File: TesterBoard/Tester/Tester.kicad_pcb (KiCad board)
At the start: 2 copper layers, 147 parts, among them J1 Conn_01x03_Pin, J2 PJ-102A, J3 Conn_01x03_Pin, J4 Conn_01x02_Pin, J5 Conn_01x02_Pin, J6 Conn_01x02_Pin, J7 Conn_01x02_Pin, J8 Conn_01x16_Pin, J9 Conn_01x08_Pin, SW1 SW_Push, SW10 SW_Push, SW2 SW_Push, SW3 SW_Push, SW4 SW_Push, SW5 SW_Push, SW6 SW_Push, SW7 SW_Push, SW8 SW_Push, U1 L7805, U10 74HC244, U2 Z80CPU, U3 74LS14, U4 sn74ls32n, U5 CY62256-70PC, U6 LCD-16X2, U7 SST39SF010, U8 74HC138, U9 74HC00, Y1 ACH-4.000MHZ-EK

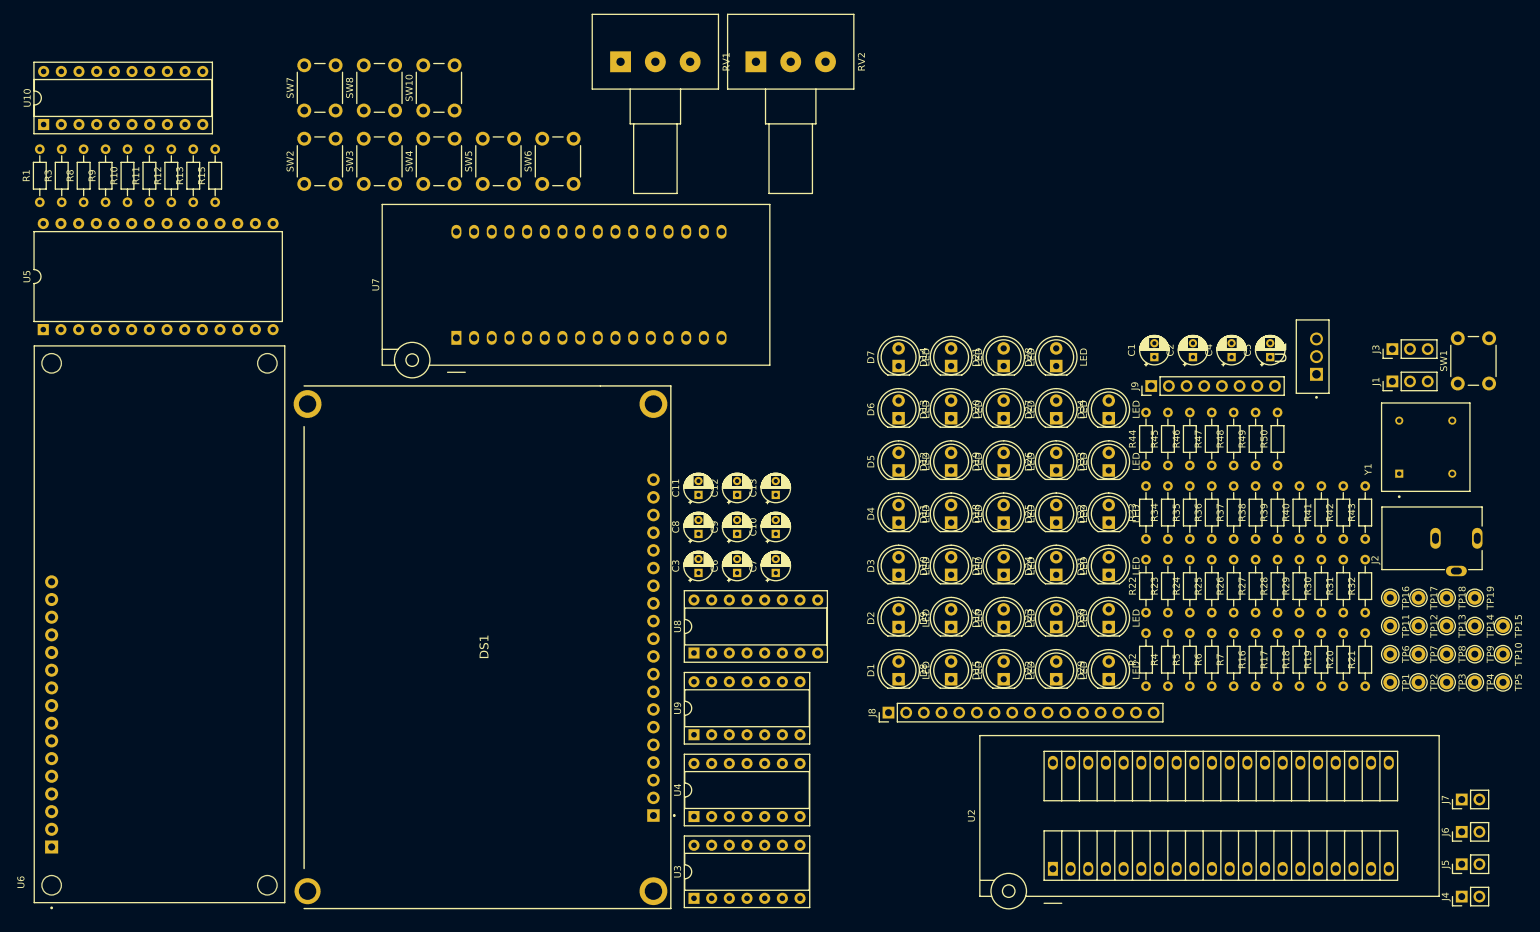
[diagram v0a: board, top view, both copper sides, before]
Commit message: updated PCB to fix logic, ready to place and route
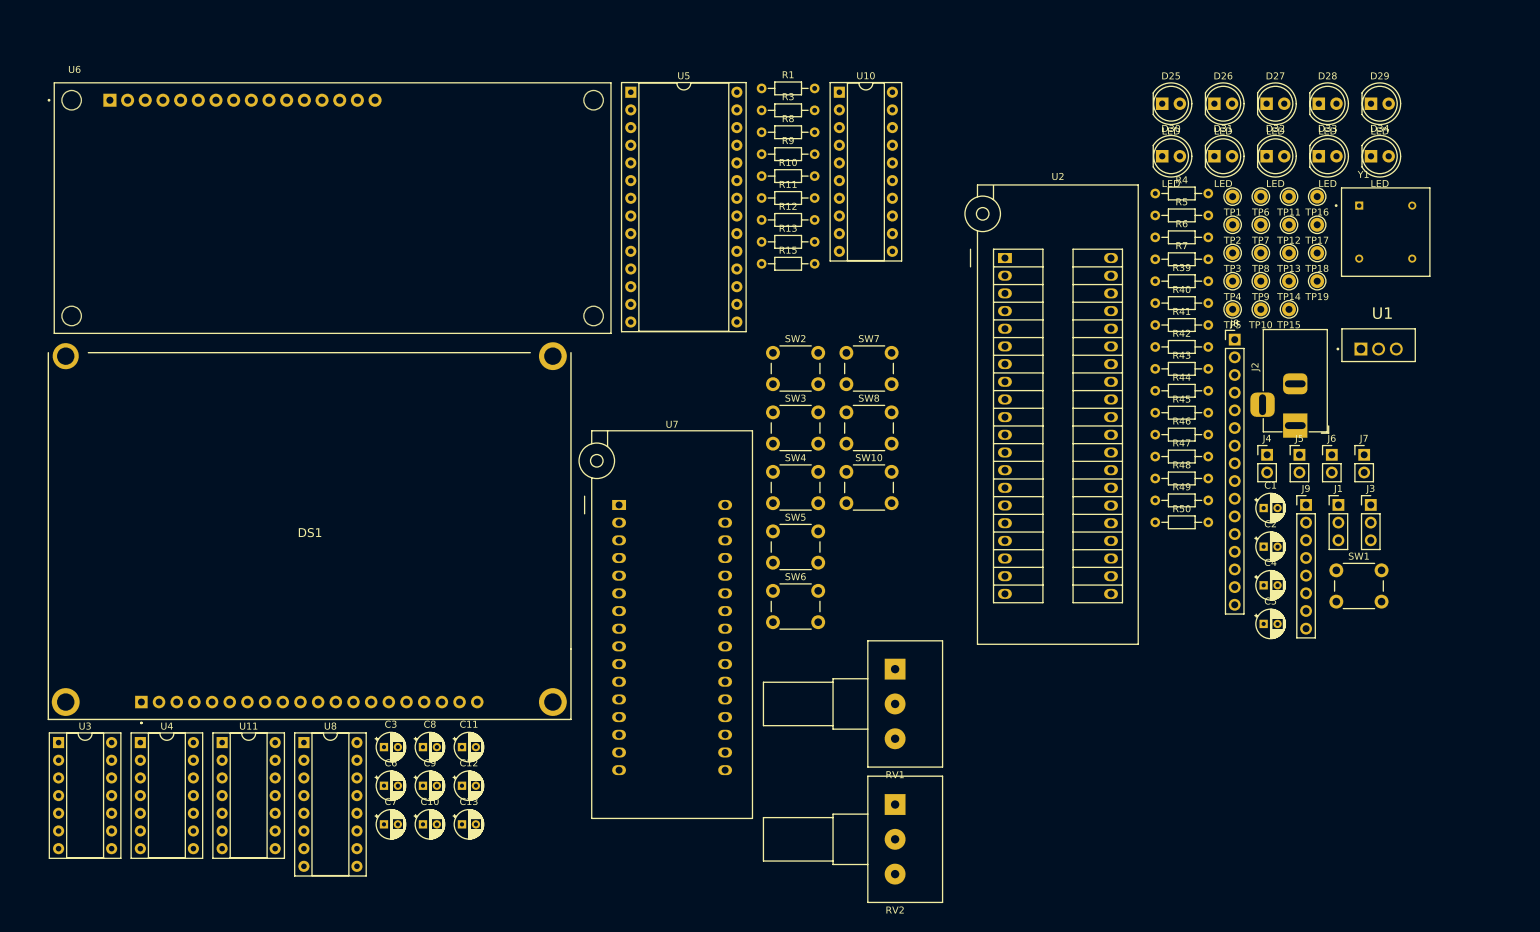
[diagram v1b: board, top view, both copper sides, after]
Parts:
- removed D1, D10, D11, D12, D13, D14, D15, D16, D17, D18, D19, D2, D20, D21, D22, D23, D24, D3, D4, D5, D6, D7, D8, D9: LED, ECE445L:LED_D5.0mm
- removed R16, R17, R18, R19, R2, R20, R21, R22, R23, R24, R25, R26, R27, R28, R29, R30, R31, R32, R33, R34, R35, R36, R37, R38: 1K, ECE445L:R_Axial_DIN0204_L3.6mm_D1.6mm_P7.62mm_Horizontal
- removed U9: 74HC00, Package_DIP:DIP-14_W7.62mm_Socket
- added U11: 74LS32, Package_DIP:DIP-14_W7.62mm_Socket, F.Cu at (69.3, 128.1)
- J2: footprint Z80_Tester_Footprints:CUI_PJ-102A -> Connector_BarrelJack:BarrelJack_Horizontal
- U4: value sn74ls32n -> 74LS02
- U5: footprint Package_DIP:DIP-28_W15.24mm -> Package_DIP:DIP-28_W15.24mm_Socket
- moved U10 114.4 mm to (158.0, 34.6), turned to 0 degrees
- moved RV2 108.6 mm to (166.0, 136.9), turned to 0 degrees
- moved R1 105.0 mm to (146.8, 34.0), turned to 0 degrees
- moved R3 101.4 mm to (146.8, 37.2), turned to 0 degrees
- moved R8 97.9 mm to (146.8, 40.4), turned to 0 degrees
- moved RV1 95.8 mm to (166.0, 117.5), turned to 0 degrees
- moved R9 94.5 mm to (146.8, 43.5), turned to 0 degrees
- moved U3 94.0 mm to (45.8, 128.1), turned to 0 degrees
- moved R10 91.2 mm to (146.8, 46.6), turned to 0 degrees
- moved U5 91.0 mm to (128.0, 34.6), turned to 0 degrees
- moved D29 90.9 mm to (234.4, 36.2), turned to 0 degrees
- moved U2 88.0 mm to (181.8, 58.4), turned to 0 degrees
- moved R11 88.0 mm to (146.8, 49.8), turned to 0 degrees
- moved SW7 85.3 mm to (159.0, 72.0), turned to 0 degrees
- moved R12 84.9 mm to (146.8, 53.0), turned to 0 degrees
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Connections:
- U4 pad 1: /WR -> 1602_Enable
- U4 pad 10: (no net) -> unconnected-(U4-Pad10)
- U4 pad 11: (no net) -> +5V
- U4 pad 12: (no net) -> +5V
- U4 pad 13: (no net) -> unconnected-(U4-Pad13)
- U4 pad 14: (no net) -> +5V
- U4 pad 2: /MREQ -> /1602_Select
- U4 pad 3: Net-(U5-~{OE}) -> /WR
- U4 pad 4: GND -> 12864_Enable
- U4 pad 5: /MREQ -> /12864_Select
- U4 pad 6: /RD -> /WR
- U4 pad 7: Net-(U5-~{WE}) -> GND
- U4 pad 9: (no net) -> +5V

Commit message: minor changes to pcb : labels for schematic
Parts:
- moved U6 182.9 mm to (-86.4, -12.0)
- moved DS1 175.8 mm to (-110.7, 71.8)
- moved C10 161.3 mm to (-58.0, 180.2)
- moved C11 161.3 mm to (-52.4, 169.1)
- moved C12 161.3 mm to (-52.4, 174.7)
- moved C13 161.3 mm to (-52.4, 180.2)
- moved C3 161.3 mm to (-63.6, 169.1)
- moved C6 161.3 mm to (-63.6, 174.7)
- moved C7 161.3 mm to (-63.6, 180.2)
- moved C8 161.3 mm to (-58.0, 169.1)
- moved C9 161.3 mm to (-58.0, 174.7)
- moved U11 161.3 mm to (-86.8, 168.5)
- moved U3 161.3 mm to (-110.3, 168.5)
- moved U4 161.3 mm to (-98.6, 168.5)
- moved U8 161.3 mm to (-75.1, 168.5)
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
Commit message: Placed PCB awaiting review
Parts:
- D25, D26, D27, D28, D29, D30, D31, D32, D33, D34, DS1, R1, R10, R11, R12, R13, R15, R39, R41, R42, R43, R44, R45, R46, R47, R48, R49, R50, R8, R9, RV1, RV2, SW1, SW10, SW2, SW3, SW4, SW5, SW6, SW7, SW8, U6: moved to B.Cu
- moved C7 312.7 mm to (205.0, 20.0)
- moved U3 307.2 mm to (169.4, 41.5)
- moved C6 296.9 mm to (223.0, 97.0)
- moved U4 277.7 mm to (171.4, 103.4)
- moved U11 267.4 mm to (148.4, 41.3)
- moved C3 258.5 mm to (153.0, 28.0)
- moved C8 257.8 mm to (153.0, 21.0)
- moved DS1 254.2 mm to (133.6, 142.0)
- moved U8 234.6 mm to (150.2, 103.1)
- moved GND 234.5 mm to (24.0, 114.0)
- moved C11 229.2 mm to (174.0, 133.0), turned to 90 degrees
- moved GND 222.4 mm to (81.0, 139.0)
- moved /Halt 217.2 mm to (79.0, 63.0)
- moved J3 214.2 mm to (23.1, 128.8), turned to 180 degrees
- moved /M1 206.8 mm to (79.0, 56.0)
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- renumbered TP4 to /Halt, TP10 to /INT, TP8 to /IOREQ, TP3 to /M1, TP7 to /MREQ, TP9 to /NMI, TP5 to /RD, TP1 to /Reset, TP11 to /WAIT, TP6 to /WR, TP19 to GND, TP18 to GND, TP14 to GND, TP17 to GND, TP12 to GND, TP16 to GND, TP13 to GND, TP15 to GND
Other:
- board outline added: 209.1 x 127 mm
- board text added: "5V Jump"
- board text added: "External 5V"
- board text added: "External Clock"
- board text added: "External GND"
- board text added: "IO 3-8 Decoder"
- board text added: "IO Enable Logic"
- board text added: "LCD"
- board text added: "Memory"
- board text added: "Oscillator"
- board text added: "Power In"
- board text added: "Reset"
- board text added: "SRAM"
- board text added: "Schmitt Trigger Inverter"
- board text added: "Unused LCD"
- board text added: "Z80"

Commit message: Almost done routing
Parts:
- added H1: ~, ECE445L:MountingHole_4_40, F.Cu at (259.2, 22.0)
- added H2: ~, ECE445L:MountingHole_4_40, F.Cu at (258.9, 150.6)
- added H3: ~, ECE445L:MountingHole_4_40, F.Cu at (24.8, 152.0)
- added H4: ~, ECE445L:MountingHole_4_40, F.Cu at (25.5, 21.9)
- moved C7 86.3 mm to (256.6, 89.3)
- moved D34 85.9 mm to (144.0, 61.2), turned to 0 degrees
- moved D31 77.6 mm to (144.1, 49.0), turned to 0 degrees
- moved D33 74.7 mm to (135.3, 61.2), turned to 0 degrees
- moved C4 72.5 mm to (136.5, 132.8), turned to 180 degrees
- moved TP17 71.6 mm to (143.2, 132.5), turned to 180 degrees
- moved D30 66.4 mm to (135.0, 49.0), turned to 0 degrees
- moved D26 62.9 mm to (125.8, 61.2), turned to 0 degrees
- moved D29 55.1 mm to (125.8, 49.0), turned to 0 degrees
- moved D32 50.8 mm to (116.0, 61.2), turned to 0 degrees
- moved TP4 44.3 mm to (117.6, 41.2)
- moved D28 43.7 mm to (116.3, 49.0), turned to 0 degrees
- moved SW8 42.8 mm to (73.5, 137.5)
- moved J1 41.6 mm to (184.4, 91.8)
- moved R40 41.6 mm to (199.2, 82.7)
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- renumbered /Reset to TP1, /INT to TP10, /WAIT to TP11, GND to TP12, GND to TP13, GND to TP14, GND to TP15, GND to TP16, GND to TP17, GND to TP18, GND to TP19, /M1 to TP3, /Halt to TP4, /RD to TP5, /WR to TP6, /MREQ to TP7, /IOREQ to TP8, /NMI to TP9
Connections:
- U3 pad 8: /Buttons_Enable -> unconnected-(U3-Pad8)
- U3 pad 9: Buttons_Enable -> +5V
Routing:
- net GND: track 0.00 -> 1171.3 mm, vias 0 -> 1
- net +5V: track 0.00 -> 954.4 mm
- net B7: track 0.00 -> 250.7 mm, vias 0 -> 7
- net Address3: track 0.00 -> 228.6 mm, vias 0 -> 1
- net /Buttons_Enable: track 0.00 -> 225.7 mm, vias 0 -> 11
- net Data4: track 0.00 -> 216.8 mm, vias 0 -> 5
- net 1602_Enable: track 0.00 -> 215.1 mm, vias 0 -> 2
- net Data5: track 0.00 -> 212.1 mm, vias 0 -> 8
- net Data7: track 0.00 -> 209.7 mm, vias 0 -> 2
- net Data6: track 0.00 -> 204.7 mm, vias 0 -> 8
- net Address14: track 0.00 -> 197.9 mm, vias 0 -> 6
- net B1: track 0.00 -> 192.9 mm, vias 0 -> 9
- net B6: track 0.00 -> 192.7 mm, vias 0 -> 6
- net Address13: track 0.00 -> 187.0 mm, vias 0 -> 7
- net Address12: track 0.00 -> 184.2 mm, vias 0 -> 6
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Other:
- board size 209.1 x 127 mm -> 246.3 x 138.9 mm
- board text added: "/Halt"
- board text added: "/INT"
- board text added: "/IOREQ"
- board text added: "/M1"
- board text added: "/MREQ"
- board text added: "/NMI"
- board text added: "/RD"
- board text added: "/WAIT"
- board text added: "/WR"

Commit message: PCB routed no errors
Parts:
- moved TP/MREQ 6.23 mm to (162.8, 27.9)
- moved TP/WR 6.01 mm to (168.8, 27.8)
- renumbered SW10 to SWB0, SW2 to SWB1, SW3 to SWB2, SW4 to SWB3, SW5 to SWB4, SW6 to SWB5, SW7 to SWB6, SW8 to SWB7, TP4 to TP/Halt, TP10 to TP/INT, TP8 to TP/IOREQ, TP3 to TP/M1, TP7 to TP/MREQ, TP9 to TP/NMI, TP5 to TP/RD, TP1 to TP/Reset, TP11 to TP/WAIT, TP6 to TP/WR, TP2 to TPClk, TP19 to TPGND, TP18 to TPGND, TP14 to TPGND, TP17 to TPGND, TP12 to TPGND, TP16 to TPGND, TP13 to TPGND, TP15 to TPGND
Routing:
- net Data0: track 145.4 -> 530.4 mm, vias 5 -> 17
- net Data2: track 153.6 -> 501.7 mm, vias 4 -> 13
- net Address4: track 88.1 -> 422.8 mm, vias 0 -> 15
- net Data6: track 204.7 -> 525.3 mm, vias 8 -> 17
- net Data5: track 212.1 -> 524.8 mm, vias 8 -> 16
- net Data1: track 145.1 -> 452.5 mm, vias 6 -> 21
- net Data7: track 209.7 -> 513.5 mm, vias 2 -> 11
- net Data4: track 216.8 -> 518.6 mm, vias 5 -> 14
- net Data3: track 176.2 -> 477.2 mm, vias 8 -> 13
- net Address3: track 228.6 -> 478.8 mm, vias 1 -> 10
- net Address2: track 92.3 -> 317.2 mm, vias 0 -> 11
- net Address1: track 94.3 -> 314.3 mm, vias 0 -> 13
- net Address5: track 84.4 -> 275.2 mm, vias 0 -> 9
- net Address6: track 80.7 -> 266.3 mm, vias 0 -> 9
- net Address0: track 96.1 -> 278.2 mm, vias 0 -> 11
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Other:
- board text added: "IH04 Z80 Drop-in Replacement Tester Board Moid Meghani 2026 Pranav Tenneti Daniel McIver Neeraj Anantha Hirsch Prasad"

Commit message: last silk screen labels added
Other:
- board text added: "12863 IO Ports: 1: Left Side CMD 9: Left Side DATA 17: Right Side CMD 25: Right Side DATA"
- board text added: "1602 IO Ports: 0: CMD 8: DATA"
- board text added: "Buttons IO Port: 2: Read Buttons"
- board text added: "ECE Senior Design 2026 - IH04 Neeraj Anantha Daniel McIver Moid Meghani Hirsch Prasad Pranav Tenneti"
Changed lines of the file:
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@@
+		)
+	)
+	(gr_text "Buttons IO Port:\n2: Read Buttons"
+		(at 80.5 99.5 270)
+		(layer "B.SilkS")
+		(effects
+			(font
+				(size 1.5 1.5)
+				(thickness 0.3)
+				(bold yes)
+			)
+			(justify left bottom mirror)
+		)
+	)
+	(gr_text "12863 IO Ports:\n1: Left Side CMD\n9: Left Side DATA\n17: Right Side CMD\n25: Right Side DATA"
+		(at 169 139 0)
+		(layer "B.SilkS")
+		(effects
+			(font
+				(size 1.5 1.5)
+				(thickness 0.3)
+				(bold yes)
+			)
+			(justify left bottom mirror)
+		)
+	)
+	(gr_text "1602 IO Ports:\n0: CMD\n8: DATA"
+		(at 52 77 -90)
+		(layer "B.SilkS")
+		(effects
+			(font
+				(size 1.5 1.5)
+				(thickness 0.3)
+				(bold yes)
+			)
+			(justify left bottom mirror)
+		)
+	)
+	(gr_text "ECE Senior Design 2026 - IH04\nNeeraj Anantha\nDaniel McIver\nMoid Meghani\nHirsch Prasad\nPranav Tenneti"
+		(at 161.5 108.5 -90)
+		(layer "B.SilkS")
+		(effects
+			(font
+				(size 1.5 1.5)
+				(thickness 0.3)
+				(bold yes)
+			)
+			(justify left bottom mirror)
 		)
 	)
